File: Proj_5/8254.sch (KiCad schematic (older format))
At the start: 1 part

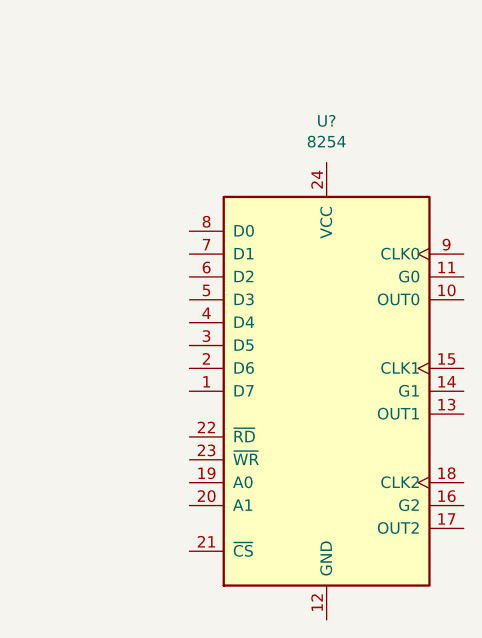
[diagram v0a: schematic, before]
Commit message: Placed 8086 in own Sheet
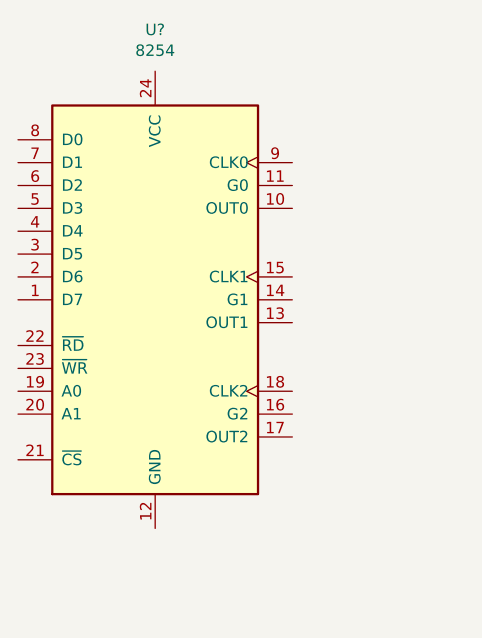
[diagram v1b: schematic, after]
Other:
- moved on the sheet: U?
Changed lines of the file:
@@
 $Descr A4 11693 8268
 encoding utf-8
-Sheet 8 9
+Sheet 8 10
 Title ""
 Date ""
@@
 L Timer:8254 U?
 U 1 1 5EA9C227
-P 6100 3650
-F 0 "U?" H 6100 4831 50  0000 C CNN
-F 1 "8254" H 6100 4740 50  0000 C CNN
-F 2 "Package_DIP:DIP-24_W15.24mm" H 6150 3900 50  0001 C CNN
-F 3 "http://www.scs.stanford.edu/10wi-cs140/pintos/specs/8254.pdf" H 5650 4550 50  0001 C CNN
-	1    6100 3650
+P 5350 3250
+F 0 "U?" H 5350 4431 50  0000 C CNN
+F 1 "8254" H 5350 4340 50  0000 C CNN
+F 2 "Package_DIP:DIP-24_W15.24mm" H 5400 3500 50  0001 C CNN
+F 3 "http://www.scs.stanford.edu/10wi-cs140/pintos/specs/8254.pdf" H 4900 4150 50  0001 C CNN
+	1    5350 3250
 	1    0    0    -1
 $EndComp
